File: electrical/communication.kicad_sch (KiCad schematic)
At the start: 23 parts

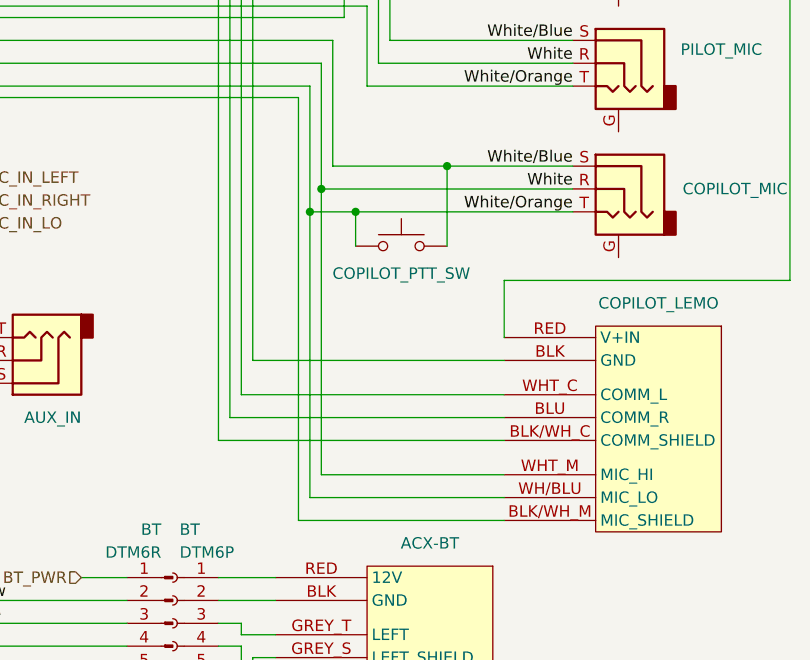
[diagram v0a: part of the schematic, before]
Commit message: Made notes about POSN+/- for Fly LED. Also, fixed Mic Lo wiring on copilot headset.
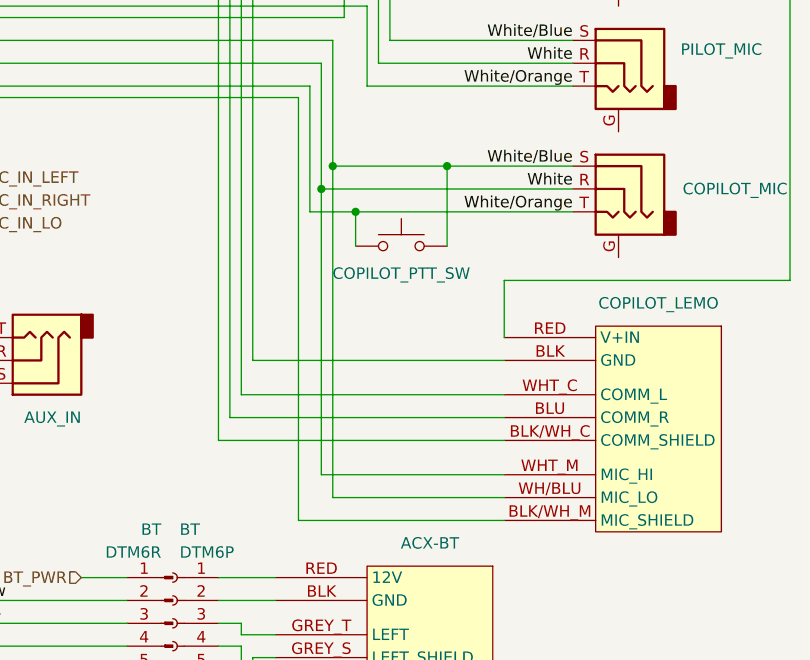
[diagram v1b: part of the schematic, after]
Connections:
- net AUDIO_IN_LO: now also COPILOT_LEMO.WH/BLU (MIC_LO)
- net White/Orange: no longer COPILOT_LEMO.WH/BLU (MIC_LO)
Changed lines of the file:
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@@
 	(title_block
 		(title "Communication")
-		(date "2026-01-09")
-		(rev "1.2.8")
+		(date "2026-01-10")
+		(rev "1.2.9")
 		(company "N877RV")
 	)
@@
 	)
 	(junction
-		(at 203.2 100.33)
-		(diameter 0)
-		(color 0 0 0 0)
-	)
-	(junction
 		(at 218.44 95.25)
 		(diameter 0)
@@
 	)
 	(junction
+		(at 205.74 95.25)
+		(diameter 0)
+		(color 0 0 0 0)
+	)
+	(junction
 		(at 204.47 97.79)
 		(diameter 0)
@@
 	(wire
 		(pts
+			(xy 205.74 95.25) (xy 205.74 132.08)
+		)
+		(stroke
+			(width 0)
+			(type default)
+		)
+	)
+	(wire
+		(pts
 			(xy 144.78 148.59) (xy 153.67 148.59)
 		)
@@
 	(wire
 		(pts
-			(xy 203.2 100.33) (xy 203.2 132.08)
-		)
-		(stroke
-			(width 0)
-			(type default)
-		)
-	)
-	(wire
-		(pts
 			(xy 204.47 129.54) (xy 224.79 129.54)
 		)
@@
 	(wire
 		(pts
-			(xy 203.2 132.08) (xy 224.79 132.08)
-		)
-		(stroke
-			(width 0)
-			(type default)
-		)
-	)
-	(wire
-		(pts
 			(xy 138.43 102.87) (xy 149.86 102.87)
 		)
@@
 		)
 		(stroke
+			(width 0)
+			(type default)
+		)
+	)
+	(wire
+		(pts
+			(xy 205.74 132.08) (xy 224.79 132.08)
+		)
+		(stroke

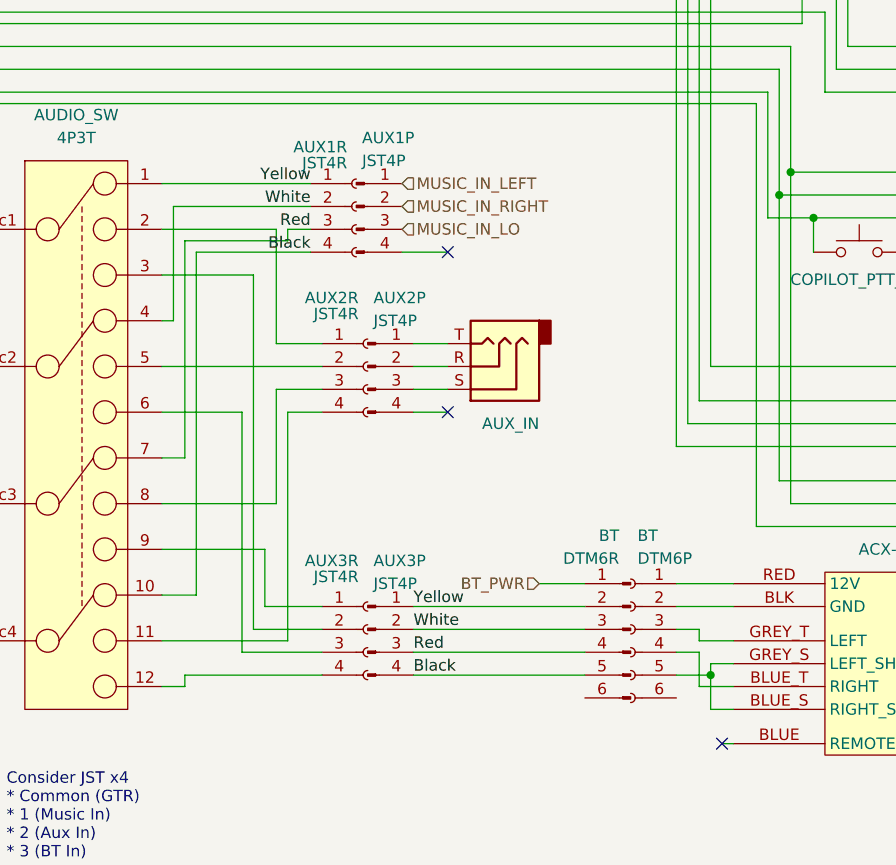
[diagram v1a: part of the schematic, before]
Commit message: Fixed colors for Aux In
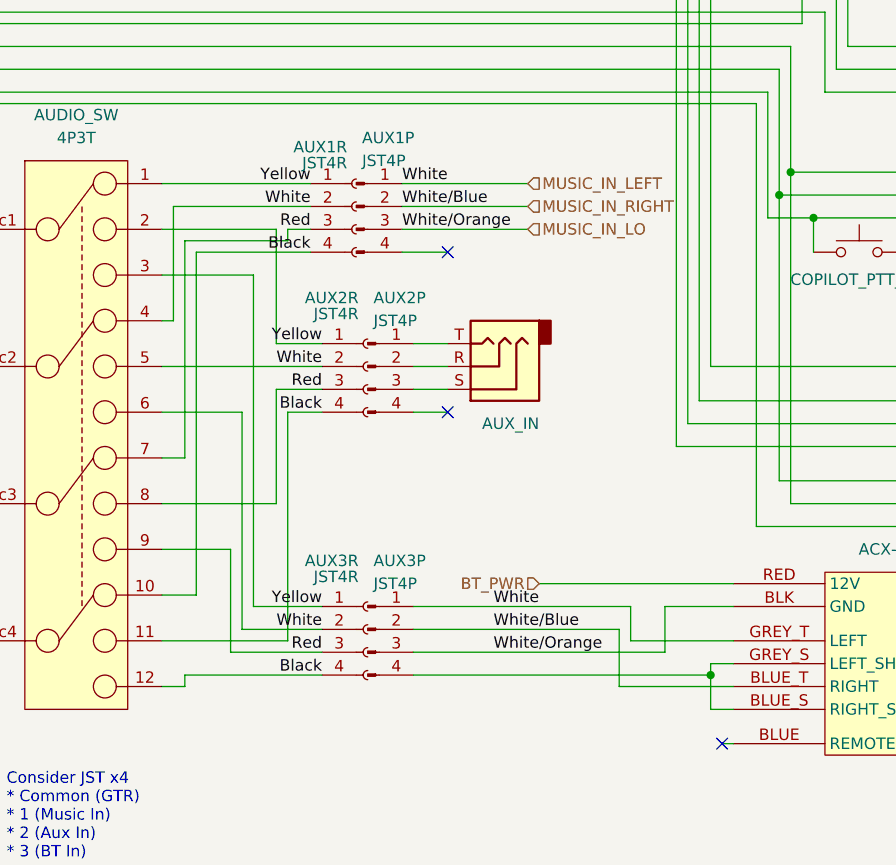
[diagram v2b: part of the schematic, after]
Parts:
- removed BT: DTM6R, symbol Connector:Conn_01x06_Pin
- removed BT: DTM6P, symbol Connector:Conn_01x06_Socket
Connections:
- net MUSIC_IN_LEFT is gone; now on net AUDIO_IN_HI: AUX1P.1 (Pin_1)
- net MUSIC_IN_RIGHT is gone; now on net AUDIO_IN_LO: AUX1P.2 (Pin_2)
- net White/Orange is gone; now on net MUSIC_IN_LO: AUXCR.3 (Pin_3), COPILOT_HS.S, COPILOT_LEMO.BLK (GND), COPILOT_MIC.T, COPILOT_PTT_SW.1, GTR20.P2001_15 (COPILOT_PTT), GTR20.P2001_30 (COPILOT_HS_LO), GTR20.P2001_33 (PILOT_HS_LO), GTR20.P2001_35 (PILOT_PTT), GTR20.P2001_37 (MUSIC_LO), PILOT_HS.S, PILOT_LEMO.BLK (GND), PILOT_MIC.T
- net AUDIO_IN_HI: now also ACX-BT.GREY_T (LEFT), AUDIO_SW.5, AUDIO_SW.6, AUX2R.2 (Pin_2), AUX3P.1 (Pin_1), AUX3R.2 (Pin_2); no longer AUX3P.2 (Pin_2)
- net AUDIO_IN_LO: now also ACX-BT.BLUE_T (RIGHT), AUX3P.2 (Pin_2)
- net BT_PWR: now also ACX-BT.RED (12V)
- net Black: now also AUDIO_SW.11, AUDIO_SW.12, AUX2R.4 (Pin_4), AUX3R.4 (Pin_4); no longer AUX3P.4 (Pin_4)
- net MUSIC_IN_LO: now also ACX-BT.BLK (GND), AUX3P.3 (Pin_3)
- net Red: now also AUDIO_SW.8, AUDIO_SW.9, AUX2R.3 (Pin_3), AUX3R.3 (Pin_3); no longer AUX3P.3 (Pin_3)
- net Yellow: now also AUDIO_SW.2, AUDIO_SW.3, AUX2R.1 (Pin_1), AUX3R.1 (Pin_1); no longer AUX3P.1 (Pin_1)
- net at ACX-BT.BLUE_S (RIGHT_SHIELD), ACX-BT.GREY_S (LEFT_SHIELD): now also AUX3P.4 (Pin_4)

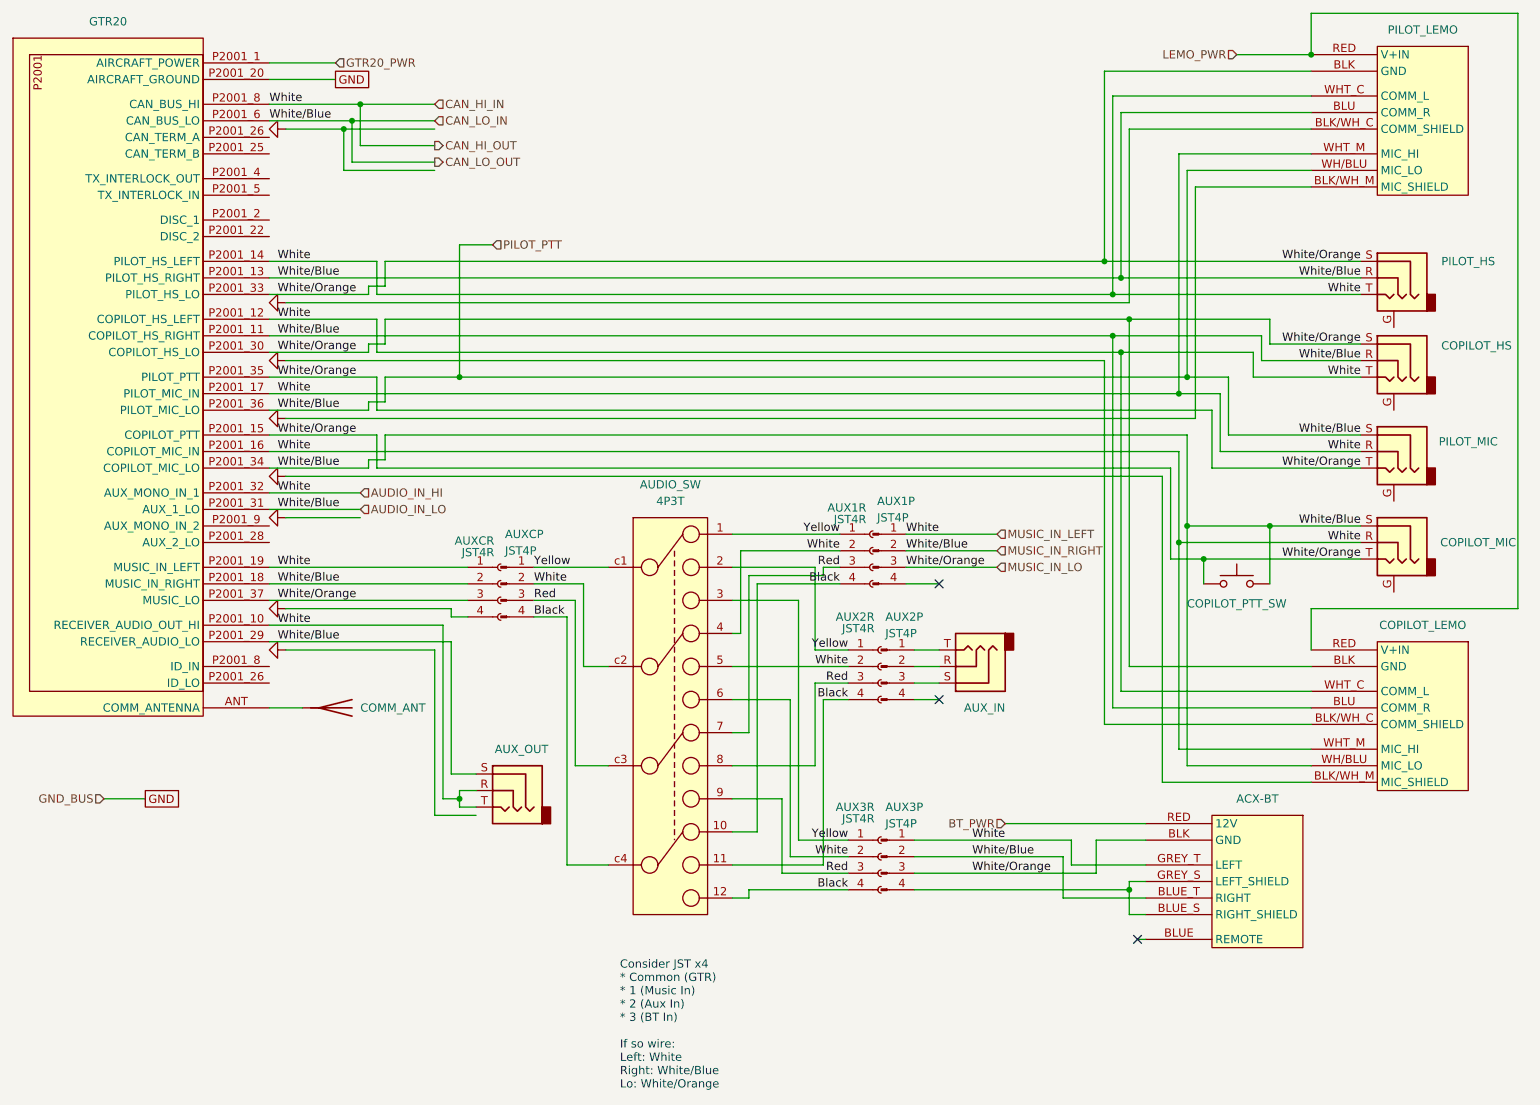
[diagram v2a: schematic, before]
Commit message: Fixed can hi pin on GTR 20. Changed how ACX-BT wires with low vs. shield. Added pitch trim colors. Removed pitch trim ground going to flaps ground. Removed extra connector on GDL 52 and changed to 4 wire shielded instead of two 2 wire shielded.
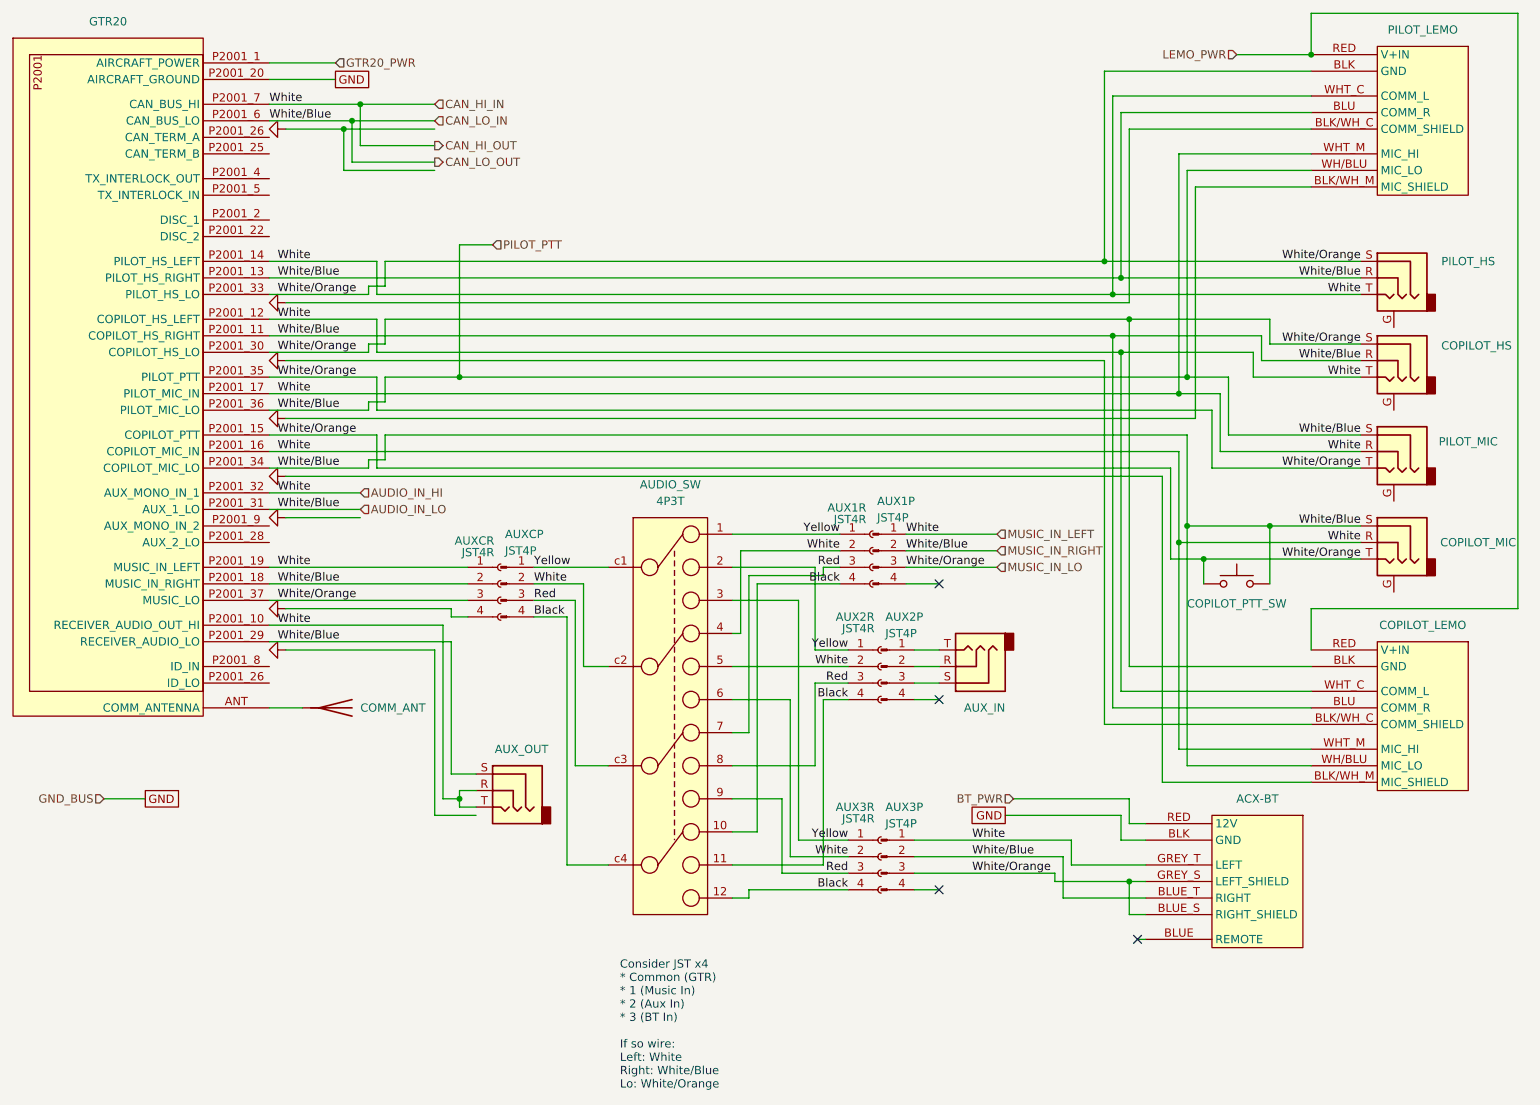
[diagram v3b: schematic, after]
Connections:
- net AUDIO_IN_HI: now also GTR20.P2001_7 (CAN_BUS_HI); no longer GTR20.P2001_8 (ID_IN)
- net GND: now also ACX-BT.BLK (GND)
- net MUSIC_IN_LO: now also ACX-BT.BLUE_S (RIGHT_SHIELD), ACX-BT.GREY_S (LEFT_SHIELD); no longer ACX-BT.BLK (GND)
- now unconnected: AUX3P.4 (Pin_4)
- no-connect marks 3 -> 4
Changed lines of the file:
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@@
 	(title_block
 		(title "Communication")
-		(date "2026-01-11")
-		(rev "1.2.10")
+		(date "2026-01-13")
+		(rev "1.2.11")
 		(company "N877RV")
 	)
@@
 	)
 	(junction
-		(at 196.85 151.13)
-		(diameter 0)
-		(color 0 0 0 0)
-	)
-	(junction
 		(at 205.74 72.39)
 		(diameter 0)
@@
 	)
 	(junction
+		(at 196.85 149.86)
+		(diameter 0)
+		(color 0 0 0 0)
+	)
+	(junction
 		(at 78.74 30.48)
 		(diameter 0)
@@
 		(at 167.64 121.92)
 	)
+	(no_connect
+		(at 167.64 151.13)
+	)
 	(wire
 		(pts
@@
 	(wire
 		(pts
-			(xy 191.77 148.59) (xy 163.83 148.59)
+			(xy 185.42 148.59) (xy 185.42 149.86)
 		)
 		(stroke
@@
 	(wire
 		(pts
+			(xy 196.85 140.97) (xy 196.85 137.16)
+		)
+		(stroke
+			(width 0)
+			(type default)
+		)
+	)
+	(wire
+		(pts
 			(xy 67.31 114.3) (xy 90.17 114.3)
 		)
@@
 	(wire
 		(pts
+			(xy 196.85 137.16) (xy 179.07 137.16)
+		)
+		(stroke
+			(width 0)
+			(type default)
+		)
+	)
+	(wire
+		(pts
 			(xy 149.86 121.92) (xy 149.86 147.32)
 		)
@@
 	(wire
 		(pts
-			(xy 196.85 151.13) (xy 196.85 149.86)
-		)
-		(stroke
-			(width 0)
-			(type dash)
-		)
-	)
-	(wire
-		(pts
-			(xy 196.85 149.86) (xy 199.39 149.86)
-		)
-		(stroke
-			(width 0)
-			(type dash)
-		)
-	)
-	(wire
-		(pts
 			(xy 39.37 137.16) (xy 45.72 137.16)
 		)
@@
 	(wire
 		(pts
+			(xy 199.39 143.51) (xy 195.58 143.51)
+		)
+		(stroke
+			(width 0)
+			(type default)
+		)
+	)
+	(wire
+		(pts
 			(xy 195.58 57.15) (xy 195.58 31.75)
 		)
@@
 	(wire
 		(pts
-			(xy 196.85 154.94) (xy 199.39 154.94)
-		)
-		(stroke
-			(width 0)
-			(type dash)
-		)
-	)
-	(wire
-		(pts
 			(xy 187.96 143.51) (xy 187.96 147.32)
 		)
@@
 	(wire
 		(pts
-			(xy 196.85 154.94) (xy 196.85 151.13)
+			(xy 176.53 99.06) (xy 162.56 99.06)
 		)
 		(stroke
 			(width 0)
-			(type dash)
+			(type default)
 		)
 	)
 	(wire
 		(pts
-			(xy 176.53 99.06) (xy 162.56 99.06)
+			(xy 215.9 68.58) (xy 215.9 72.39)
 		)
 		(stroke
@@
 	(wire
 		(pts
-			(xy 215.9 68.58) (xy 215.9 72.39)
+			(xy 185.42 149.86) (xy 196.85 149.86)
+		)
+		(stroke
+			(width 0)
+			(type default)
+		)
+	)
+	(wire
+		(pts
+			(xy 163.83 148.59) (xy 185.42 148.59)
 		)
 		(stroke
@@
 	(wire
 		(pts
-			(xy 111.76 132.08) (xy 116.84 132.08)
+			(xy 196.85 149.86) (xy 199.39 149.86)
 		)
 		(stroke
@@
 	(wire
 		(pts
-			(xy 194.31 59.69) (xy 232.41 59.69)
+			(xy 111.76 132.08) (xy 116.84 132.08)
 		)
 		(stroke
@@
 	(wire
 		(pts
-			(xy 203.2 86.36) (xy 203.2 100.33)
+			(xy 194.31 59.69) (xy 232.41 59.69)
 		)
 		(stroke
@@
 	(wire
 		(pts
-			(xy 139.7 104.14) (xy 152.4 104.14)
+			(xy 203.2 86.36) (xy 203.2 100.33)
 		)
 		(stroke
 			(width 0)
-			(type dash)
+			(type default)
 		)
 	)
 	(wire
 		(pts
-			(xy 218.44 63.5) (xy 218.44 67.31)
+			(xy 139.7 104.14) (xy 152.4 104.14)
 		)
 		(stroke
 			(width 0)
-			(type default)
+			(type dash)
 		)
 	)
 	(wire
 		(pts
-			(xy 163.83 151.13) (xy 196.85 151.13)
+			(xy 218.44 63.5) (xy 218.44 67.31)
 		)
 		(stroke
 			(width 0)
-			(type dash)
+			(type default)
 		)
 	)
@@
 	(wire
 		(pts
-			(xy 177.8 140.97) (xy 199.39 140.97)
-		)
-		(stroke
-			(width 0)
-			(type default)
-		)
-	)
-	(wire
-		(pts
 			(xy 149.86 102.87) (xy 149.86 101.6)
 		)
@@
 	(wire
 		(pts
-			(xy 193.04 25.4) (xy 224.79 25.4)
+			(xy 163.83 151.13) (xy 167.64 151.13)
 		)
 		(stroke
 			(width 0)
-			(type default)
+			(type dash)
 		)
 	)
 	(wire
 		(pts
-			(xy 80.01 77.47) (xy 80.01 76.2)
+			(xy 193.04 25.4) (xy 224.79 25.4)
 		)
 		(stroke
@@
 	(wire
 		(pts
-			(xy 64.77 86.36) (xy 80.01 86.36)
+			(xy 80.01 77.47) (xy 80.01 76.2)
 		)
 		(stroke
@@
 	(wire
 		(pts
-			(xy 193.04 54.61) (xy 232.41 54.61)
+			(xy 64.77 86.36) (xy 80.01 86.36)
 		)
 		(stroke
@@
 	(wire
 		(pts
-			(xy 199.39 143.51) (xy 191.77 143.51)
+			(xy 193.04 54.61) (xy 232.41 54.61)
 		)
 		(stroke
@@
 	(wire
 		(pts
+			(xy 195.58 143.51) (xy 195.58 139.7)
+		)
+		(stroke
+			(width 0)
+			(type default)
+		)
+	)
+	(wire
+		(pts
 			(xy 92.71 107.95) (xy 67.31 107.95)
 		)
@@
 	(wire
 		(pts
+			(xy 195.58 139.7) (xy 177.8 139.7)
+		)
+		(stroke
+			(width 0)
+			(type default)
+		)
+	)
+	(wire
+		(pts
 			(xy 64.77 101.6) (xy 95.25 101.6)
 		)
@@
 	(wire
 		(pts
+			(xy 196.85 149.86) (xy 196.85 154.94)
+		)
+		(stroke
+			(width 0)
+			(type default)
+		)
+	)
+	(wire
+		(pts
 			(xy 64.77 81.28) (xy 81.28 81.28)
 		)
@@
 	(wire
 		(pts
-			(xy 191.77 143.51) (xy 191.77 148.59)
+			(xy 196.85 116.84) (xy 224.79 116.84)
 		)
 		(stroke
@@
 	(wire
 		(pts
-			(xy 196.85 116.84) (xy 224.79 116.84)
+			(xy 152.4 96.52) (xy 135.89 96.52)
 		)
 		(stroke
@@
 	(wire
 		(pts
-			(xy 152.4 96.52) (xy 135.89 96.52)
+			(xy 217.17 66.04) (xy 217.17 69.85)
 		)
 		(stroke
@@
 	(wire
 		(pts
-			(xy 217.17 66.04) (xy 217.17 69.85)
+			(xy 110.49 109.22) (xy 110.49 147.32)
 		)
 		(stroke
 			(width 0)
-			(type default)
+			(type dash)
 		)
 	)
 	(wire
 		(pts
-			(xy 110.49 109.22) (xy 110.49 147.32)
+			(xy 196.85 140.97) (xy 199.39 140.97)
 		)
 		(stroke
 			(width 0)
-			(type dash)
+			(type default)
 		)
 	)
@@
 	(wire
 		(pts
+			(xy 196.85 154.94) (xy 199.39 154.94)
+		)
+		(stroke
+			(width 0)
+			(type default)
+		)
+	)
+	(wire
+		(pts
 			(xy 193.04 54.61) (xy 193.04 25.4)
 		)
@@
 	(global_label "GND"
 		(shape passive)
+		(at 177.8 139.7 180)
+		(fields_autoplaced yes)
+		(effects
+			(font
+				(size 1.27 1.27)
+			)
+			(justify right)
+		)
+		(property "Intersheetrefs" "${INTERSHEET_REFS}"
+			(at 172.0556 139.7 0)
+			(effects
+				(font
+					(size 1.27 1.27)
+				)
+				(justify right)
+				(hide yes)
+			)
+		)
+	)
+	(global_label "GND"
+		(shape passive)
 		(at 74.93 26.67 0)
 		(fields_autoplaced yes)
@@
 	(hierarchical_label "BT_PWR"
 		(shape input)
-		(at 177.8 140.97 180)
+		(at 179.07 137.16 180)
 		(effects
 			(font
@@
 		(pin "P2001_8"
 		)
-		(pin "P2001_8"
+		(pin "P2001_7"
 		)
 		(pin "P2001_9"
